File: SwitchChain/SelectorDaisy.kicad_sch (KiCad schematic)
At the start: 2 parts, among them U201 74HC00, U202 74HC74

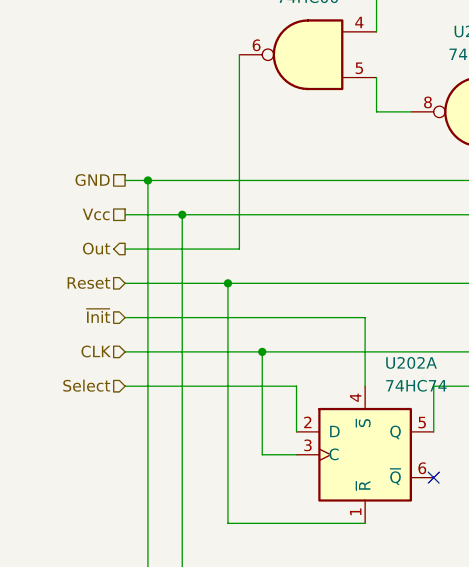
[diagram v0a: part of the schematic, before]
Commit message: fix pin label, reduce column keys to 4
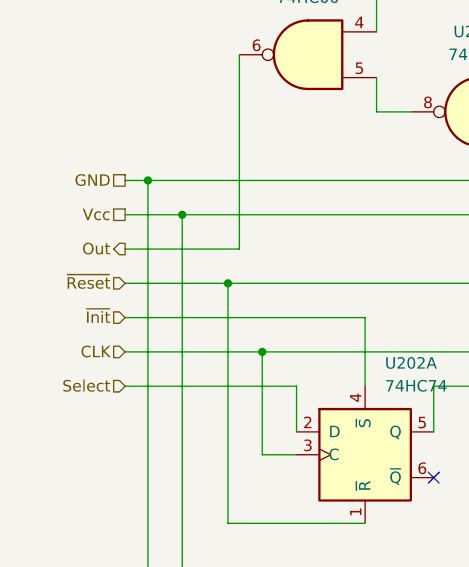
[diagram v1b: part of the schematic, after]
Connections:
- net Reset renamed ~{Reset}
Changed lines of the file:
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@@
 		)
 	)
-	(hierarchical_label "Reset"
+	(hierarchical_label "~{Reset}"
 		(shape input)
 		(at 69.85 73.66 180)
@@
 					(unit 5)
 				)
-				(path "/bdfc27f9-2f87-4fe7-a85f-b21fa09d30f0/253992b3-02ab-4aad-9a1e-d76b1438e691/26301dba-533b-46ba-8510-3ef352a12ed2"
-					(reference "U1101")
-					(unit 5)
-				)
 				(path "/bdfc27f9-2f87-4fe7-a85f-b21fa09d30f0/95715d47-4288-4034-bf4d-8592fbea460b/26301dba-533b-46ba-8510-3ef352a12ed2"
 					(reference "U601")
@@
 				(path "/bdfc27f9-2f87-4fe7-a85f-b21fa09d30f0/1ab69dab-5bac-40ee-8e89-7d9f544d3dd1/26301dba-533b-46ba-8510-3ef352a12ed2"
 					(reference "U402")
-					(unit 3)
-				)
-				(path "/bdfc27f9-2f87-4fe7-a85f-b21fa09d30f0/253992b3-02ab-4aad-9a1e-d76b1438e691/26301dba-533b-46ba-8510-3ef352a12ed2"
-					(reference "U1102")
 					(unit 3)
 				)
@@
 					(unit 1)
 				)
-				(path "/bdfc27f9-2f87-4fe7-a85f-b21fa09d30f0/253992b3-02ab-4aad-9a1e-d76b1438e691/26301dba-533b-46ba-8510-3ef352a12ed2"
-					(reference "U1101")
-					(unit 1)
-				)
 				(path "/bdfc27f9-2f87-4fe7-a85f-b21fa09d30f0/95715d47-4288-4034-bf4d-8592fbea460b/26301dba-533b-46ba-8510-3ef352a12ed2"
 					(reference "U601")
@@
 					(unit 1)
 				)
-				(path "/bdfc27f9-2f87-4fe7-a85f-b21fa09d30f0/253992b3-02ab-4aad-9a1e-d76b1438e691/26301dba-533b-46ba-8510-3ef352a12ed2"
-					(reference "U1102")
-					(unit 1)
-				)
 				(path "/bdfc27f9-2f87-4fe7-a85f-b21fa09d30f0/95715d47-4288-4034-bf4d-8592fbea460b/26301dba-533b-46ba-8510-3ef352a12ed2"
 					(reference "U602")
@@
 					(unit 4)
 				)
-				(path "/bdfc27f9-2f87-4fe7-a85f-b21fa09d30f0/253992b3-02ab-4aad-9a1e-d76b1438e691/26301dba-533b-46ba-8510-3ef352a12ed2"
-					(reference "U1101")
-					(unit 4)
-				)
 				(path "/bdfc27f9-2f87-4fe7-a85f-b21fa09d30f0/95715d47-4288-4034-bf4d-8592fbea460b/26301dba-533b-46ba-8510-3ef352a12ed2"
 					(reference "U601")
@@
 				(path "/bdfc27f9-2f87-4fe7-a85f-b21fa09d30f0/1ab69dab-5bac-40ee-8e89-7d9f544d3dd1/26301dba-533b-46ba-8510-3ef352a12ed2"
 					(reference "U402")
-					(unit 2)
-				)
-				(path "/bdfc27f9-2f87-4fe7-a85f-b21fa09d30f0/253992b3-02ab-4aad-9a1e-d76b1438e691/26301dba-533b-46ba-8510-3ef352a12ed2"
-					(reference "U1102")
 					(unit 2)
 				)
@@
 					(unit 3)
 				)
-				(path "/bdfc27f9-2f87-4fe7-a85f-b21fa09d30f0/253992b3-02ab-4aad-9a1e-d76b1438e691/26301dba-533b-46ba-8510-3ef352a12ed2"
-					(reference "U1101")
-					(unit 3)
-				)
 				(path "/bdfc27f9-2f87-4fe7-a85f-b21fa09d30f0/95715d47-4288-4034-bf4d-8592fbea460b/26301dba-533b-46ba-8510-3ef352a12ed2"
 					(reference "U601")
@@
 					(unit 2)
 				)
-				(path "/bdfc27f9-2f87-4fe7-a85f-b21fa09d30f0/253992b3-02ab-4aad-9a1e-d76b1438e691/26301dba-533b-46ba-8510-3ef352a12ed2"
-					(reference "U1101")
-					(unit 2)
-				)

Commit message: change connector
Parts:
- U201: Manufacturer Part number (none) -> SN74HCS00BQAR; Original (none) -> N; Purchase Link (none) -> https://www.digikey.com/en/products/detail/texas-instrument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
- U202: Manufacturer Part number (none) -> SN74HCS74BQAR; Original (none) -> N; Purchase Link (none) -> https://www.digikey.com/en/products/detail/texas-instrument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
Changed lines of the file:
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@@
+			)
+		)
+		(property "Manufacturer Part number" "SN74HCS00BQAR"
+			(at 86.36 130.81 0)
+			(effects
+				(font
+					(size 1.27 1.27)
+				)
+				(hide yes)
+			)
+		)
+		(property "Original" "N"
+			(at 86.36 130.81 0)
+			(effects
+				(font
+					(size 1.27 1.27)
+				)
+				(hide yes)
+			)
+		)
+		(property "Purchase Link" "https://www.digikey.com/en/products/detail/texas-instruments/SN74HCS00BQAR/13896419"
+			(at 86.36 130.81 0)
+			(effects
+				(font
+					(size 1.27 1.27)
+				)
+				(hide yes)
 			)
 		)
@@
 			)
 		)
+		(property "Manufacturer Part number" "SN74HCS74BQAR"
+			(at 107.95 130.81 0)
+			(effects
+				(font
+					(size 1.27 1.27)
+				)
+				(hide yes)
+			)
+		)
+		(property "Original" "N"
+			(at 107.95 130.81 0)
+			(effects
+				(font
+					(size 1.27 1.27)
+				)
+				(hide yes)
+			)
+		)
+		(property "Purchase Link" "https://www.digikey.com/en/products/detail/texas-instruments/SN74HCS74BQAR/13896426"
+			(at 107.95 130.81 0)
+			(effects
+				(font
+					(size 1.27 1.27)
+				)
+				(hide yes)
+			)
+		)
 		(pin "6"
 		)
@@
 			)
 		)
+		(property "Manufacturer Part number" "SN74HCS00BQAR"
+			(at 114.3 41.91 0)
+			(effects
+				(font
+					(size 1.27 1.27)
+				)
+				(hide yes)
+			)
+		)
+		(property "Original" "N"
+			(at 114.3 41.91 0)
+			(effects
+				(font
+					(size 1.27 1.27)
+				)
+				(hide yes)
+			)
+		)
+		(property "Purchase Link" "https://www.digikey.com/en/products/detail/texas-instruments/SN74HCS00BQAR/13896419"
+			(at 114.3 41.91 0)
+			(effects
+				(font
+					(size 1.27 1.27)
+				)
+				(hide yes)
+			)
+		)
 		(pin "9"
 		)
@@
 			)
 		)
+		(property "Manufacturer Part number" "SN74HCS74BQAR"
+			(at 96.52 92.71 0)
+			(effects
+				(font
+					(size 1.27 1.27)
+				)
+				(hide yes)
+			)
+		)
+		(property "Original" "N"
+			(at 96.52 92.71 0)
+			(effects
+				(font
+					(size 1.27 1.27)
+				)
+				(hide yes)
+			)
+		)
+		(property "Purchase Link" "https://www.digikey.com/en/products/detail/texas-instruments/SN74HCS74BQAR/13896426"
+			(at 96.52 92.71 0)
+			(effects
+				(font
+					(size 1.27 1.27)
+				)
+				(hide yes)
+			)
+		)
 		(pin "6"
 		)
@@
 			)
 		)
+		(property "Manufacturer Part number" "SN74HCS00BQAR"
+			(at 161.29 130.81 0)
+			(effects
+				(font
+					(size 1.27 1.27)
+				)
+				(hide yes)
+			)
+		)
+		(property "Original" "N"
+			(at 161.29 130.81 0)
+			(effects
+				(font
+					(size 1.27 1.27)
+				)
+				(hide yes)
+			)
+		)
+		(property "Purchase Link" "https://www.digikey.com/en/products/detail/texas-instruments/SN74HCS00BQAR/13896419"
+			(at 161.29 130.81 0)
+			(effects
+				(font
+					(size 1.27 1.27)
+				)
+				(hide yes)
+			)
+		)
 		(pin "9"
 		)
@@
 			)
 		)
+		(property "Manufacturer Part number" "SN74HCS74BQAR"
+			(at 138.43 130.81 0)
+			(effects
+				(font
+					(size 1.27 1.27)
+				)
+				(hide yes)
+			)
+		)
+		(property "Original" "N"
+			(at 138.43 130.81 0)
+			(effects
+				(font
+					(size 1.27 1.27)
+				)
+				(hide yes)
+			)
+		)
+		(property "Purchase Link" "https://www.digikey.com/en/products/detail/texas-instruments/SN74HCS74BQAR/13896426"
+			(at 138.43 130.81 0)
+			(effects
+				(font
+					(size 1.27 1.27)
+				)
+				(hide yes)
+			)
+		)
 		(pin "6"
 		)
@@
 			)
 		)
+		(property "Manufacturer Part number" "SN74HCS00BQAR"
+			(at 109.22 54.61 0)
+			(effects
+				(font
+					(size 1.27 1.27)
+				)
+				(hide yes)
+			)
+		)
+		(property "Original" "N"
+			(at 109.22 54.61 0)
+			(effects
+				(font
+					(size 1.27 1.27)
+				)
+				(hide yes)
+			)
+		)
+		(property "Purchase Link" "https://www.digikey.com/en/products/detail/texas-instruments/SN74HCS00BQAR/13896419"
+			(at 109.22 54.61 0)
+			(effects
+				(font
+					(size 1.27 1.27)
+				)
+				(hide yes)
+			)
+		)
 		(pin "9"
 		)
@@
 			(at 90.17 48.26 0)
 			(effects
+				(font
+					(size 1.27 1.27)
+				)
+				(hide yes)
+			)
+		)
+		(property "Manufacturer Part number" "SN74HCS00BQAR"
+			(at 90.17 48.26 0)
+			(effects
+				(font
+					(size 1.27 1.27)
+				)
+				(hide yes)
+			)
+		)
+		(property "Original" "N"
+			(at 90.17 48.26 0)
+			(effects
+				(font
+					(size 1.27 1.27)
+				)
+				(hide yes)
+			)
+		)
+		(property "Purchase Link" "https://www.digikey.com/en/products/detail/texas-instruments/SN74HCS00BQAR/13896419"
+			(at 90.17 48.26 0)
+			(effects
